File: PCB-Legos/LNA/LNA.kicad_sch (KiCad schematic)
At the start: 36 parts, among them J1 Conn_Coaxial, J2 Conn_Coaxial, J3 Conn_Coaxial, U1 LP2985XX-N, U2 LNA-TP3M9037, U3 QPQ1907, U4 LP2985XX-N, U5 LNA-TP3M9037, U6 QPQ1907

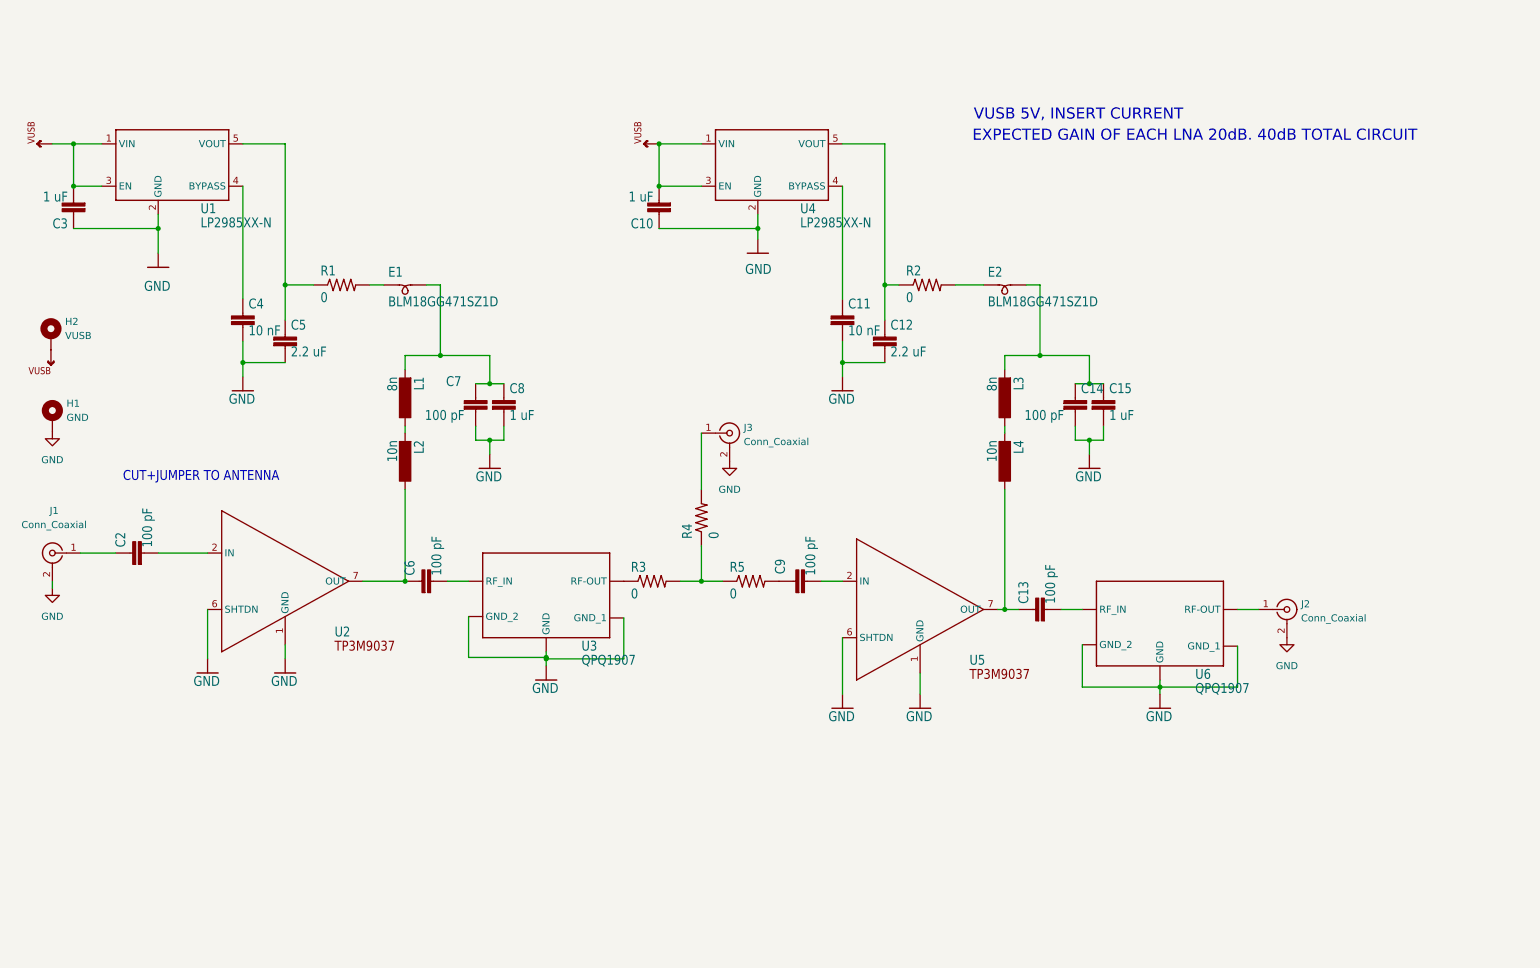
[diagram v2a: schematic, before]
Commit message: LNA Test Board
LNA test board with ability to test each of two stages.
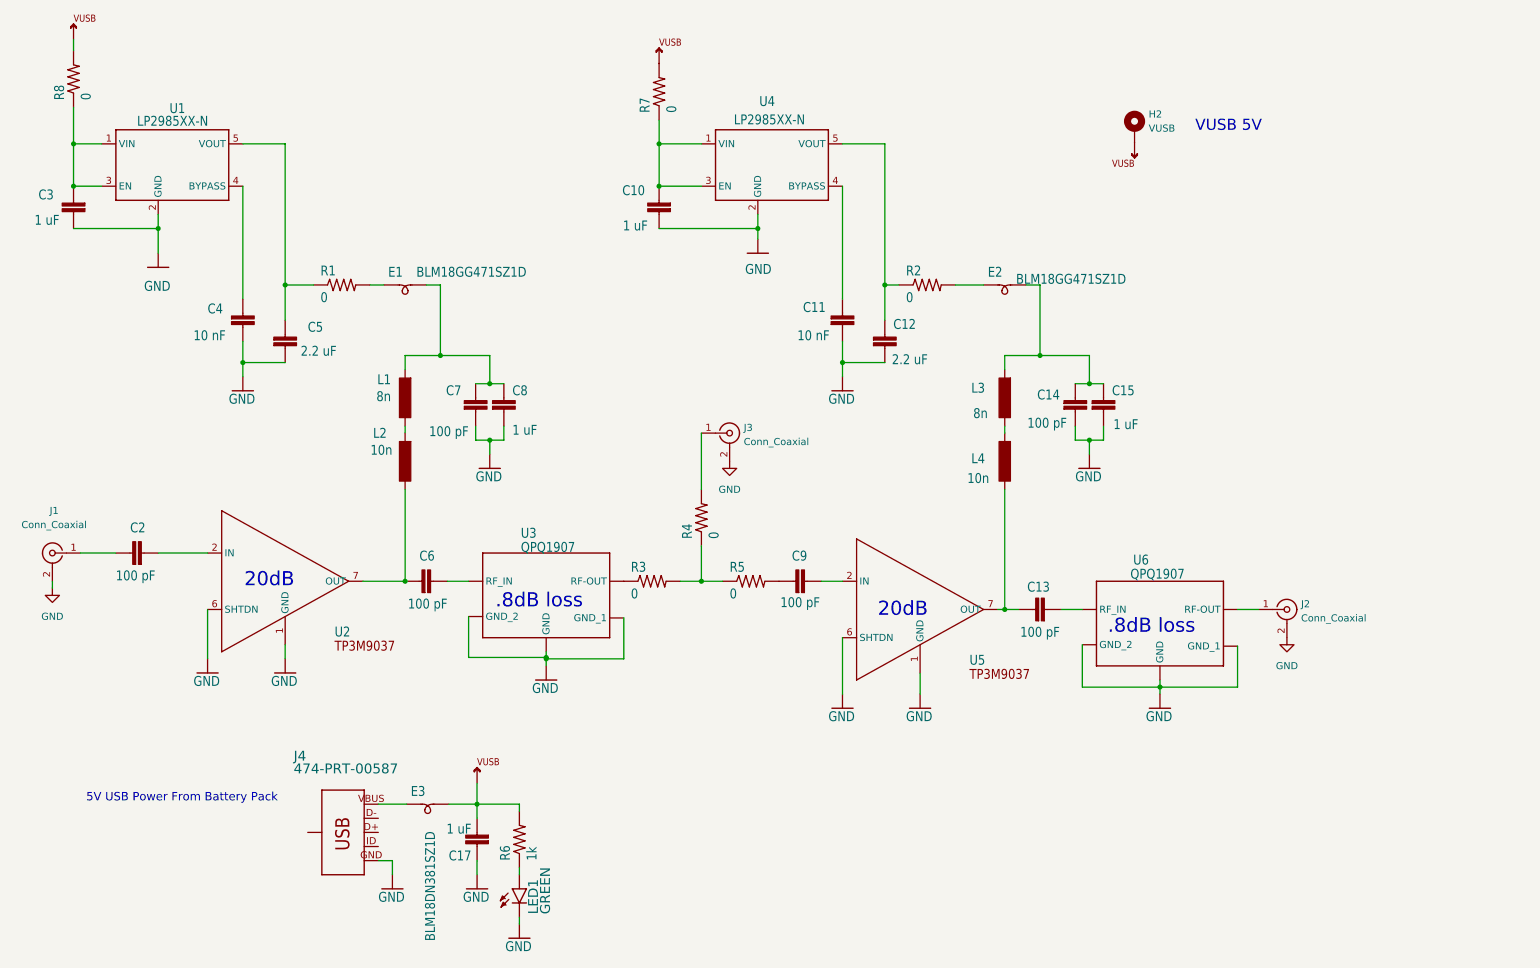
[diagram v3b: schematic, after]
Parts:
- removed H1: GND, Connector_PinHeader_2.00mm:PinHeader_1x01_P2.00mm_Vertical, symbol Mechanical:MountingHole_Pad
- added C17: 1 uF, HGS_Reflector:.0603-B-NOSILK, symbol HGS_Reflector-eagle-import:C-EU0603-B-NOSILK
- added E3: BLM18DN381SZ1D, HGS_Reflector:.0603-B, symbol HGS_Reflector-eagle-import:L-BEAD-0603-B
- added J4: 474-PRT-00587, HGS_Reflector:USB-MINIB, symbol HGS_Reflector-eagle-import:USB_MINI-B_SMT
- added LED1: GREEN, HGS_Reflector:LED-0603, symbol HGS_Reflector-eagle-import:LED-GREEN0603
- added R6: 1k, HGS_Reflector:.0603-B-NOSILK, symbol HGS_Reflector-eagle-import:R-US_0603-B-NOSILK
- added R7, R8: 0, HGS_Reflector:.0603-B-NOSILK, symbol HGS_Reflector-eagle-import:R-US_0603-B-NOSILK
- H2: footprint Connector_PinHeader_2.00mm:PinHeader_1x01_P2.00mm_Vertical -> Connector_PinHeader_2.54mm:PinHeader_1x02_P2.54mm_Vertical
- J1, J2, J3: footprint Connector_Coaxial:SMA_Molex_73251-1153_EdgeMount_Horizontal -> Connector_Coaxial:SMA_Amphenol_132289_EdgeMount; M/N (none) -> 142-0701-806
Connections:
- net GND: now also C17.1, J4.GND, LED1.C
- net VUSB: now also C17.2, E3.2, R6.2, R7.2, R8.2; no longer C10.2, C3.2, U1.1 (VIN), U1.3 (EN), U4.1 (VIN), U4.3 (EN)
- new net: E3.1, J4.VBUS
- new net: C10.2, R7.1, U4.1 (VIN), U4.3 (EN)
- new net: LED1.A, R6.1
- new net: C3.2, R8.1, U1.1 (VIN), U1.3 (EN)
- new net: J4.S1 (SHIELD), J4.S2 (SHIELD), J4.S3 (SHIELD), J4.S4 (SHIELD)
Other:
- note added: ".8dB loss"
- note added: "20dB"
- note added: "5V USB Power From Battery Pack"
- note added: "VUSB 5V"
- note removed: "CUT+JUMPER TO ANTENNA"
- note removed: "EXPECTED GAIN OF EACH LNA 20dB. 40dB TOTAL CIRCUIT"
- note removed: "VUSB 5V, INSERT CURRENT"
- moved on the sheet: H2
